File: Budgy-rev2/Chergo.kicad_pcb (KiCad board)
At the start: 2 copper layers, 124 x 102 mm, 40 parts, among them K1 KEYSW, K10 KEYSW, K11 KEYSW, K12 KEYSW, K13 KEYSW, K14 KEYSW, K15 KEYSW, K16 KEYSW, K17 KEYSW, K2 KEYSW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

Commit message: changed to 5v for rgbled
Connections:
- LED1 pad 1: 3v3 -> 5v
- LED10 pad 1: 3v3 -> 5v
- LED11 pad 1: 3v3 -> 5v
- LED12 pad 1: 3v3 -> 5v
- LED13 pad 1: 3v3 -> 5v
- LED14 pad 1: 3v3 -> 5v
- LED15 pad 1: 3v3 -> 5v
- LED16 pad 1: 3v3 -> 5v
- LED17 pad 1: 3v3 -> 5v
- LED2 pad 1: 3v3 -> 5v
- LED3 pad 1: 3v3 -> 5v
- LED4 pad 1: 3v3 -> 5v
- LED5 pad 1: 3v3 -> 5v
- LED6 pad 1: 3v3 -> 5v
- LED7 pad 1: 3v3 -> 5v
- LED8 pad 1: 3v3 -> 5v
- LED9 pad 1: 3v3 -> 5v
- U1 pad 40: unconnected-(U1-Pad40) -> 5v
- U2 pad 1: 3v3 -> 5v
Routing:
- net 5v: track 0.00 -> 614.6 mm, vias 0 -> 43
- net 3v3: track 616.8 -> 25.4 mm, vias 43 -> 0
- net unconnected-(U1-Pad40): track 21.1 -> 0.00 mm

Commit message: added fill zones
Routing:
- added copper zone on B.Cu, net (none)
- added copper zone on F.Cu, net (none)
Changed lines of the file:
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@@
   (segment (start 167.976169 126.511785) (end 171.754977 122.732977) (width 0.25) (layer "B.Cu") (net 57))
   (segment (start 164.95 78.6255) (end 166.161011 79.836511) (width 0.25) (layer "B.Cu") (net 57))
+  (zone (net 0) (net_name "") (layers F&B.Cu) (hatch edge 0.508)
+    (connect_pads (clearance 0.508))
+    (min_thickness 0.254) (filled_areas_thickness no)
+    (fill yes (thermal_gap 0.508) (thermal_bridge_width 0.508))
+    (polygon
+      (pts
+        (xy 197.104 103.886)
+        (xy 178.562 144.018)
+        (xy 56.642 125.73)
+        (xy 53.34 26.416)
+        (xy 195.58 25.654)
+      )
+    )
+  )
 )

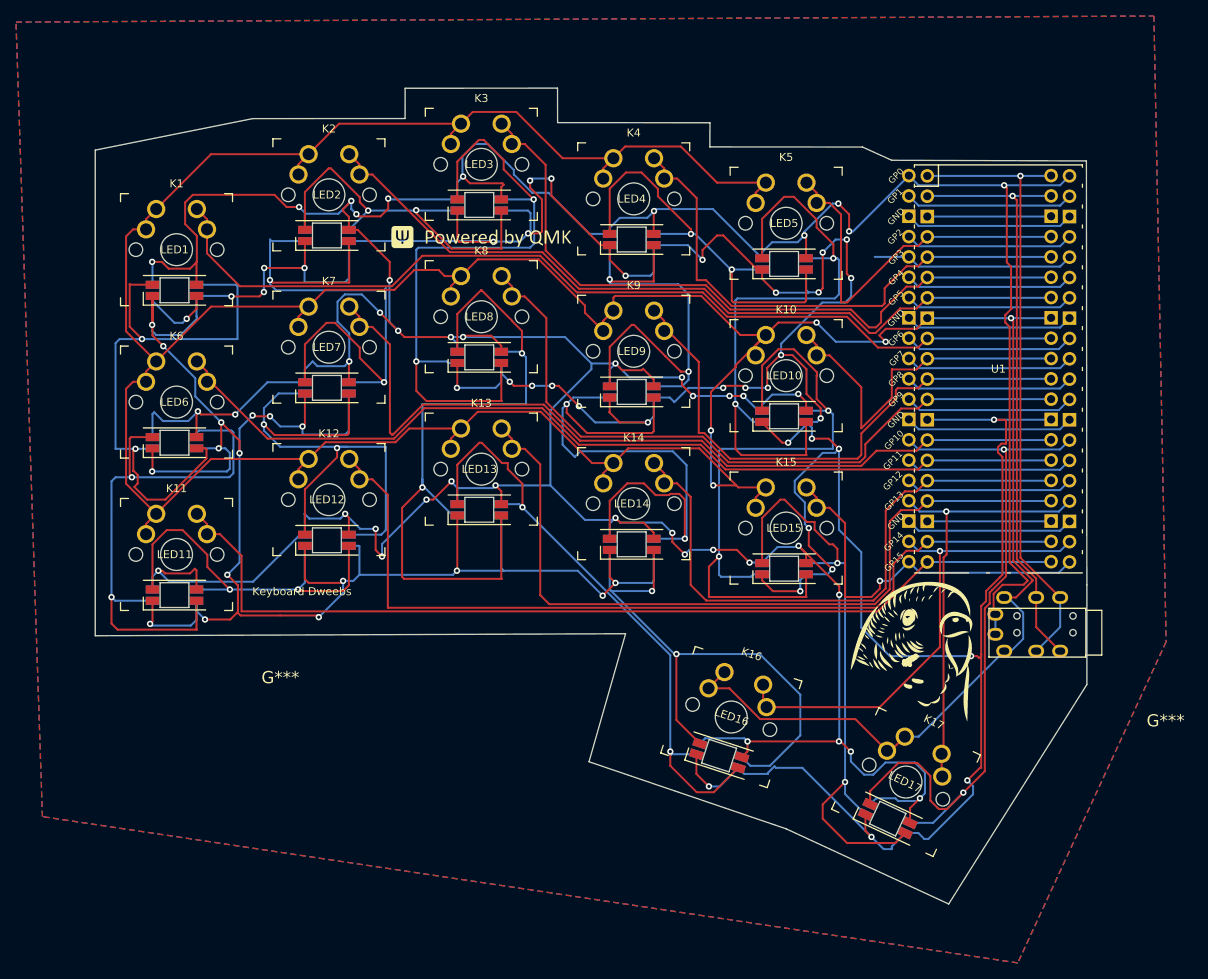
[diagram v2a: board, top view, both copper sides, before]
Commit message: add voltage divider
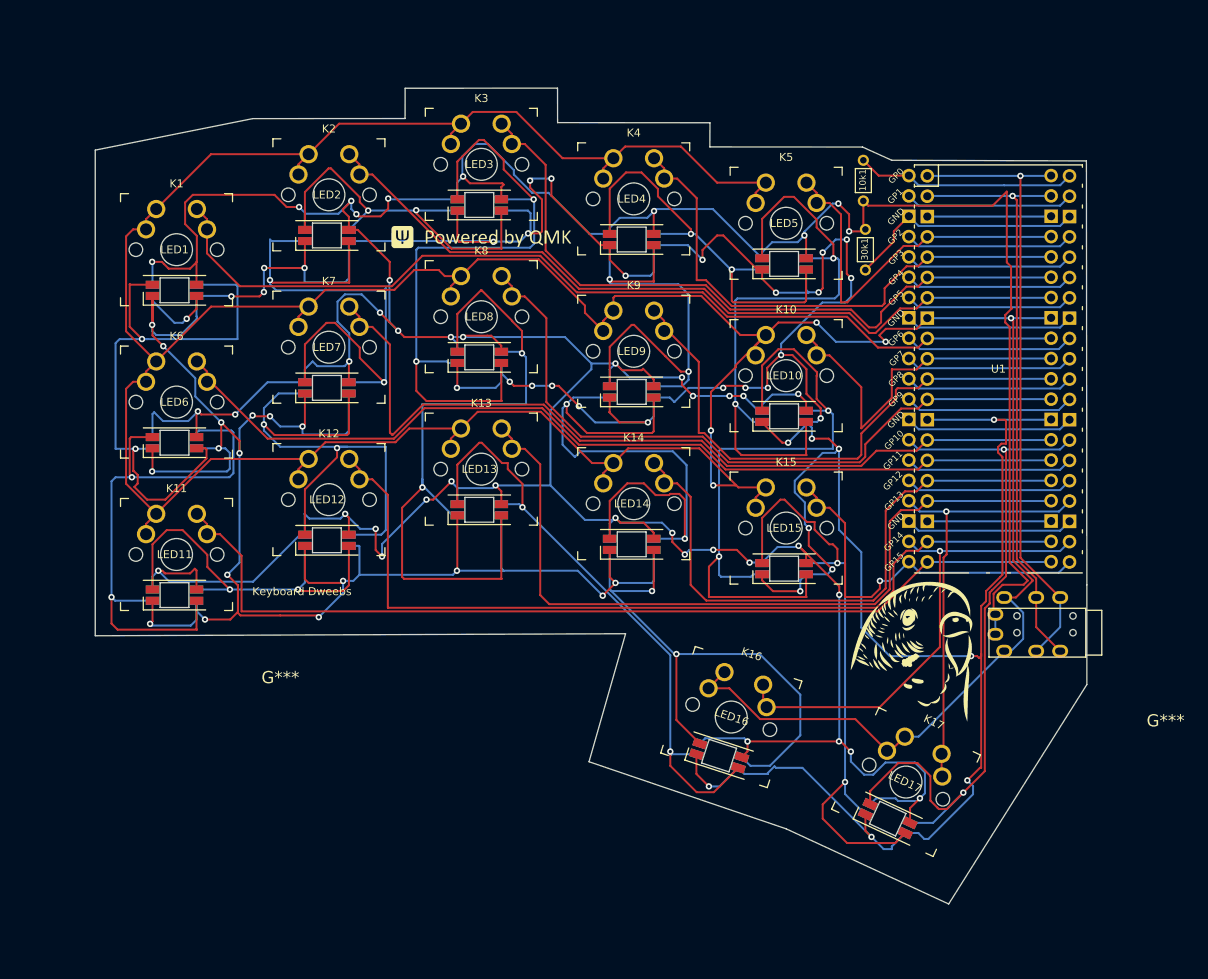
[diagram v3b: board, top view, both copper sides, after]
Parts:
- added 10k1: R, kbd:R, F.Cu at (159.3, 46.2)
- added 30k1: R, kbd:R, F.Cu at (159.5, 54.9)
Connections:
- U1 pad 38: unconnected-(U1-Pad38) -> Net-(30k1-Pad1)
- U1 pad 40: 5v -> Net-(10k1-Pad2)
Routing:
- net Net-(30k1-Pad1): track 0.00 -> 30.0 mm
- net Net-(10k1-Pad2): track 0.00 -> 27.6 mm
- net unconnected-(U1-Pad38): track 21.1 -> 0.00 mm
- net 5v: track 614.6 -> 607.4 mm, vias 43 -> 42
- net 3v3: track 25.4 -> 21.1 mm
- removed copper zone on B.Cu, net (none)
- removed copper zone on F.Cu, net (none)

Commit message: updates to rev2
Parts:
- removed 10k1, 30k1: R, kbd:R
- added U3: SN74LVC1T45DCK, Keebio-Parts:SOT-363_SC-70-6, F.Cu at (151.9, 102.9)
- added U4: SN74LVC1T45DCK, Keebio-Parts:SOT-363_SC-70-6, B.Cu at (151.9, 102.9)
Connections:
- LED17 pad 4: LED -> LED5V
- U1 pad 27: LED -> LED3V
- U1 pad 38: Net-(30k1-Pad1) -> unconnected-(U1-Pad38)
- U1 pad 40: Net-(10k1-Pad2) -> 5v
- U2 pad 1: 5v -> 3v3
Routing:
- net 3v3: track 21.1 -> 160.8 mm, vias 0 -> 5
- net LED: track 94.3 -> 0.00 mm, vias 2 -> 0
- net LED5V: track 0.00 -> 90.8 mm, vias 0 -> 4
- net LED3V: track 0.00 -> 61.4 mm, vias 0 -> 4
- net 5v: track 607.4 -> 566.0 mm, vias 42 -> 43
- net unconnected-(U1-Pad38): track 0.00 -> 30.0 mm
- net Net-(30k1-Pad1): track 30.0 -> 0.00 mm
- net Net-(10k1-Pad2): track 27.6 -> 0.00 mm
- net GND3: track 0.00 -> 1.90 mm, vias 0 -> 1
